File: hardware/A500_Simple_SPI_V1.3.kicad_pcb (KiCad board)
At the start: 2 copper layers, 41.3 x 110.5 mm, 26 parts, among them J1 68K_Host_Interface, J2 Conn_LAN_Module, J3 Conn_SD_Module, J4 Conn_SD_ACT_LED, U1 MC68000, U2 DG412, U3 74LVC00, U5 74LVC32, U6 74LVC74, U7 74LVC02

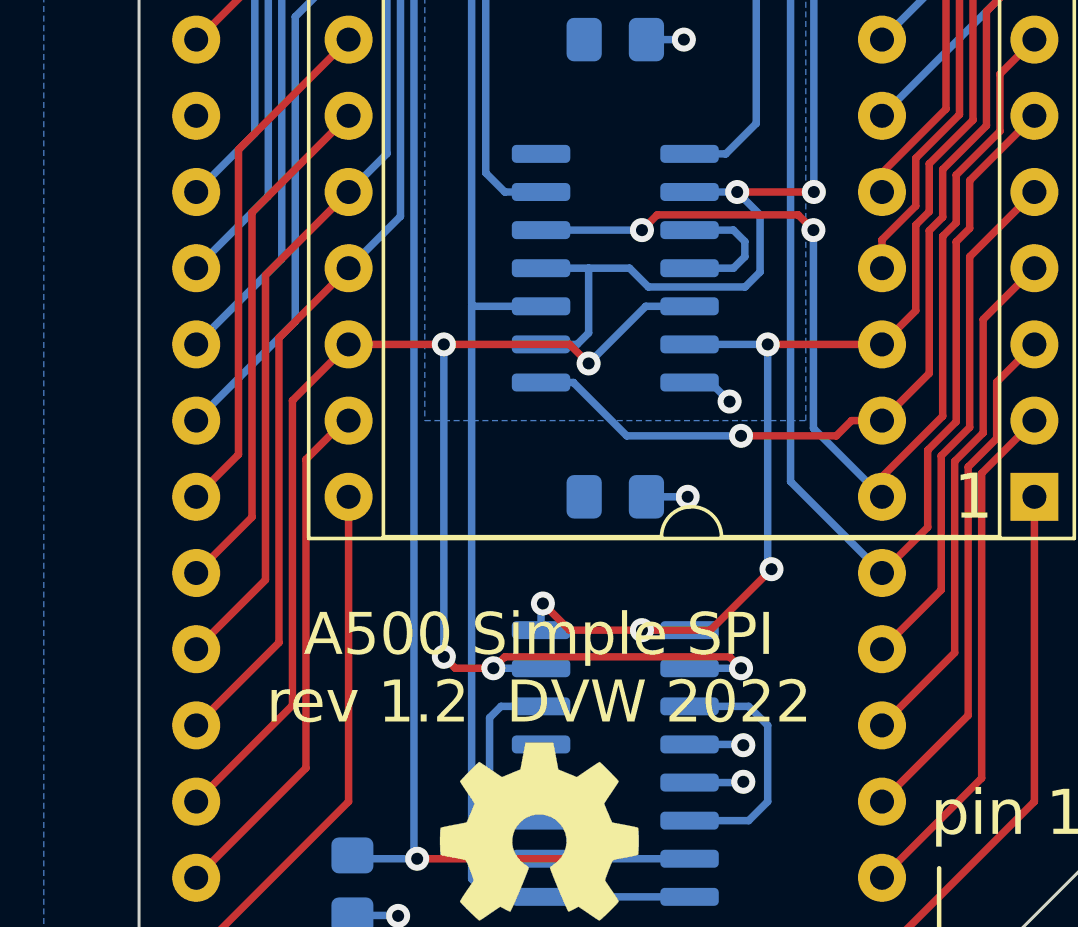
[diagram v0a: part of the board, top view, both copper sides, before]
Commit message: New Revision 1.3 which improves MOSI setup times on reads
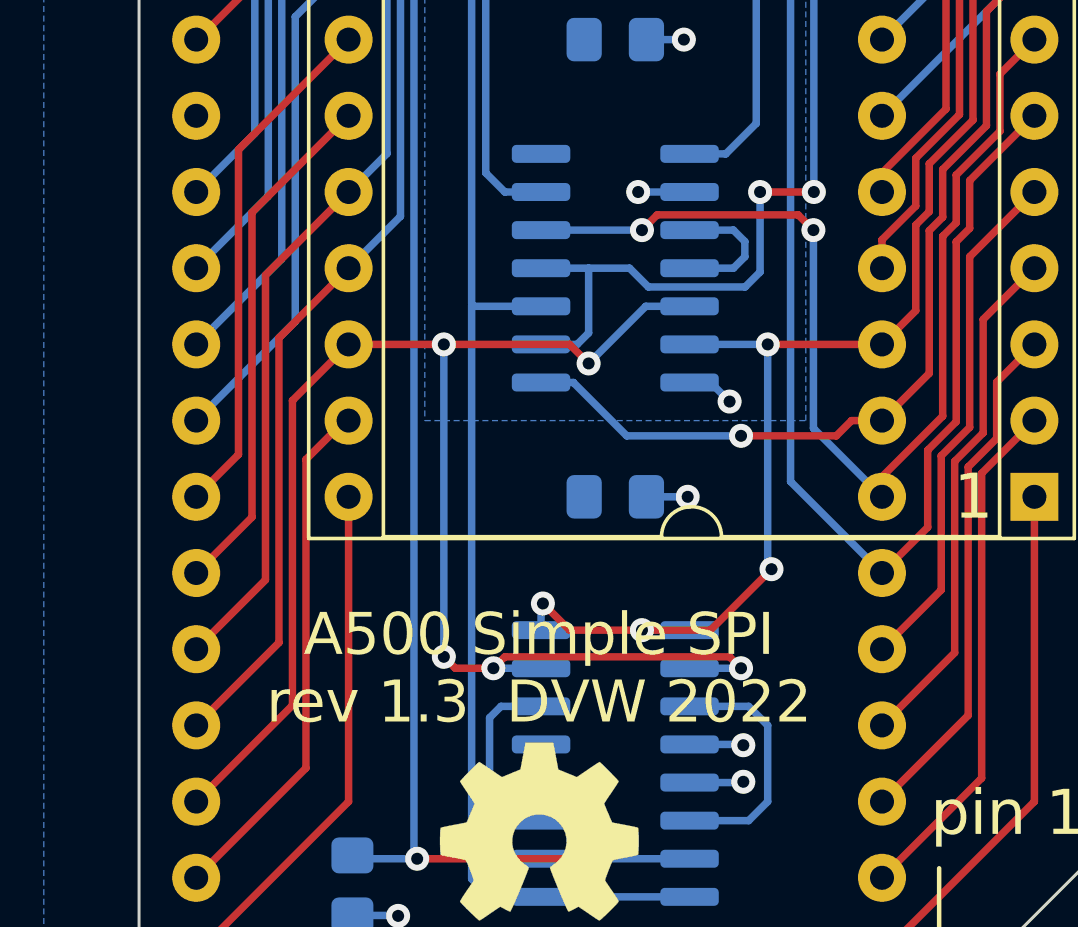
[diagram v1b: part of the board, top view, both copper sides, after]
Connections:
- U7 pad 2: ~{DECODE} -> GND
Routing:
- net ~{DECODE}: track 71.1 -> 68.5 mm
- net GND: track 24.7 -> 26.4 mm, vias 13 -> 14
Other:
- board text added: "A500 Simple SPI rev 1.3 DVW 2022"
- board text removed: "A500 Simple SPI rev 1.2 DVW 2022"
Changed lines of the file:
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@@
   (title_block
     (title "A500 Simple SPI Controller")
-    (date "2022-11-16")
-    (rev "1.2")
+    (date "2022-12-05")
+    (rev "1.3")
     (company "Dennis van Weeren")
   )
@@
     (descr "64-lead though-hole mounted DIP package, row spacing 22.86 mm (900 mils), Socket")
     (tags "THT DIP DIL PDIP 2.54mm 22.86mm 900mil Socket")
-    (property "Sheetfile" "File: A500_Simple_SPI_V1.2.kicad_sch")
+    (property "Sheetfile" "File: A500_Simple_SPI_V1.3.kicad_sch")
     (property "Sheetname" "")
     (attr through_hole)
@@
     (descr "Capacitor SMD 0805 (2012 Metric), square (rectangular) end terminal, IPC_7351 nominal with elongated pad for handsoldering. (Body size source: IPC-SM-782 page 76, https://www.pcb-3d.com/wordpress/wp-content/uploads/ipc-sm-782a_amendment_1_and_2.pdf, https://docs.google.com/spreadsheets/d/1BsfQQcO9C6DZCsRaXUlFlo91Tg2WpOkGARC1WS5S8t0/edit?usp=sharing), generated with kicad-footprint-generator")
     (tags "capacitor handsolder")
-    (property "Sheetfile" "File: A500_Simple_SPI_V1.2.kicad_sch")
+    (property "Sheetfile" "File: A500_Simple_SPI_V1.3.kicad_sch")
     (property "Sheetname" "")
     (attr smd)
@@
     (descr "Capacitor SMD 0805 (2012 Metric), square (rectangular) end terminal, IPC_7351 nominal with elongated pad for handsoldering. (Body size source: IPC-SM-782 page 76, https://www.pcb-3d.com/wordpress/wp-content/uploads/ipc-sm-782a_amendment_1_and_2.pdf, https://docs.google.com/spreadsheets/d/1BsfQQcO9C6DZCsRaXUlFlo91Tg2WpOkGARC1WS5S8t0/edit?usp=sharing), generated with kicad-footprint-generator")
     (tags "capacitor handsolder")
-    (property "Sheetfile" "File: A500_Simple_SPI_V1.2.kicad_sch")
+    (property "Sheetfile" "File: A500_Simple_SPI_V1.3.kicad_sch")
     (property "Sheetname" "")
     (attr smd)
@@
       (net 72 "Net-(R3-Pad1)") (pintype "output"))
     (pad "2" smd roundrect (at -2.475 2.54 180) (size 1.95 0.6) (layers "B.Cu" "B.Paste" "B.Mask") (roundrect_rratio 0.25)
-      (net 82 "~{DECODE}") (pintype "input"))
+      (net 1 "GND") (pintype "input"))
     (pad "3" smd roundrect (at -2.475 1.27 180) (size 1.95 0.6) (layers "B.Cu" "B.Paste" "B.Mask") (roundrect_rratio 0.25)
       (net 77 "Net-(U7-Pad3)") (pintype "input"))
@@
     (descr "64-lead though-hole mounted DIP package, row spacing 22.86 mm (900 mils), Socket")
     (tags "THT DIP DIL PDIP 2.54mm 22.86mm 900mil Socket")
-    (property "Sheetfile" "File: A500_Simple_SPI_V1.2.kicad_sch")
+    (property "Sheetfile" "File: A500_Simple_SPI_V1.3.kicad_sch")
     (property "Sheetname" "")
     (attr through_hole)
@@
     (effects (font (size 1 1) (thickness 0.15)) (justify left))
   )
-  (gr_text "A500 Simple SPI \nrev 1.2  DVW 2022" (at 171.45 127.635) (layer "F.SilkS")
+  (gr_text "A500 Simple SPI \nrev 1.3  DVW 2022" (at 171.45 127.635) (layer "F.SilkS")
     (effects (font (size 1.4 1.4) (thickness 0.3)))
   )
   (via (at 178.2572 130.2004) (size 0.8) (drill 0.4) (layers "F.Cu" "B.Cu") (net 1))
+  (via (at 174.752 111.76) (size 0.8) (drill 0.4) (layers "F.Cu" "B.Cu") (net 1))
   (via (at 177.922356 73.147356) (size 0.8) (drill 0.4) (layers "F.Cu" "B.Cu") (net 1))
   (via (at 177.8 103.505) (size 0.8) (drill 0.4) (layers "F.Cu" "B.Cu") (net 1))
@@
   (segment (start 186.267 85.3225) (end 187.7695 83.82) (width 0.25) (layer "B.Cu") (net 1))
   (segment (start 176.465 118.11) (end 177.165 118.11) (width 0.25) (layer "B.Cu") (net 1))
+  (segment (start 176.465 111.76) (end 174.752 111.76) (width 0.25) (layer "B.Cu") (net 1))
   (segment (start 162.9156 94.0015) (end 165.0785 94.0015) (width 0.25) (layer "B.Cu") (net 1))
   (segment (start 175.0275 106.68) (end 176.276 106.68) (width 0.25) (layer "B.Cu") (net 1))
@@
   (segment (start 174.879 82.55) (end 176.465 82.55) (width 0.25) (layer "B.Cu") (net 81))
   (segment (start 174.879 67.31) (end 175.133 67.564) (width 0.25) (layer "F.Cu") (net 82))
+  (segment (start 180.6085 111.76) (end 178.816 111.76) (width 0.25) (layer "F.Cu") (net 82))
   (segment (start 179.725718 67.564) (end 179.990001 67.299717) (width 0.25) (layer "F.Cu") (net 82))
   (segment (start 175.133 67.564) (end 179.725718 67.564) (width 0.25) (layer "F.Cu") (net 82))
-  (segment (start 180.6085 111.76) (end 178.054 111.76) (width 0.25) (layer "F.Cu") (net 82))
   (via (at 180.6085 111.76) (size 0.8) (drill 0.4) (layers "F.Cu" "B.Cu") (net 82))
   (via (at 179.990001 67.299717) (size 0.8) (drill 0.4) (layers "F.Cu" "B.Cu") (net 82))
   (via (at 174.879 67.31) (size 0.8) (drill 0.4) (layers "F.Cu" "B.Cu") (net 82))
-  (via (at 178.054 111.76) (size 0.8) (drill 0.4) (layers "F.Cu" "B.Cu") (net 82))
+  (via (at 178.816 111.76) (size 0.8) (drill 0.4) (layers "F.Cu" "B.Cu") (net 82))
+  (segment (start 174.467624 114.3) (end 173.101 114.3) (width 0.25) (layer "B.Cu") (net 82))
   (segment (start 173.101 114.3) (end 171.515 114.3) (width 0.25) (layer "B.Cu") (net 82))
   (segment (start 176.465 67.31) (end 174.879 67.31) (width 0.25) (layer "B.Cu") (net 82))
   (segment (start 180.015096 67.299717) (end 179.990001 67.299717) (width 0.25) (layer "B.Cu") (net 82))
+  (segment (start 178.816 111.76) (end 178.816 114.427) (width 0.25) (layer "B.Cu") (net 82))
   (segment (start 173.101 116.459) (end 172.72 116.84) (width 0.25) (layer "B.Cu") (net 82))
-  (segment (start 175.092624 114.925) (end 174.467624 114.3) (width 0.25) (layer "B.Cu") (net 82))
   (segment (start 180.6085 111.76) (end 180.6085 96.130869) (width 0.25) (layer "B.Cu") (net 82))
-  (segment (start 178.816 114.427) (end 178.318 114.925) (width 0.25) (layer "B.Cu") (net 82))
+  (segment (start 178.318 114.925) (end 175.092624 114.925) (width 0.25) (layer "B.Cu") (net 82))
   (segment (start 181.465504 95.273865) (end 181.465504 68.750125) (width 0.25) (layer "B.Cu") (net 82))
   (segment (start 181.465504 68.750125) (end 180.015096 67.299717) (width 0.25) (layer "B.Cu") (net 82))
-  (segment (start 178.054 111.76) (end 176.465 111.76) (width 0.25) (layer "B.Cu") (net 82))
   (segment (start 180.6085 96.130869) (end 181.465504 95.273865) (width 0.25) (layer "B.Cu") (net 82))
-  (segment (start 178.816 112.522) (end 178.816 114.427) (width 0.25) (layer "B.Cu") (net 82))
   (segment (start 173.101 114.3) (end 173.101 116.459) (width 0.25) (layer "B.Cu") (net 82))
   (segment (start 172.72 116.84) (end 171.515 116.84) (width 0.25) (layer "B.Cu") (net 82))
-  (segment (start 178.054 111.76) (end 178.816 112.522) (width 0.25) (layer "B.Cu") (net 82))
-  (segment (start 178.318 114.925) (end 175.092624 114.925) (width 0.25) (layer "B.Cu") (net 82))
-  (segment (start 174.467624 114.3) (end 173.101 114.3) (width 0.25) (layer "B.Cu") (net 82))
+  (segment (start 178.816 114.427) (end 178.318 114.925) (width 0.25) (layer "B.Cu") (net 82))
+  (segment (start 175.092624 114.925) (end 174.467624 114.3) (width 0.25) (layer "B.Cu") (net 82))
   (segment (start 173.101 98.425) (end 173.101 99.06) (width 0.25) (layer "F.Cu") (net 83))
   (segment (start 173.736 97.79) (end 173.101 98.425) (width 0.25) (layer "F.Cu") (net 83))
